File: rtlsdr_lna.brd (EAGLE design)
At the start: 34.6 x 11.7 mm, 18 parts, among them U1 MIC5205-3

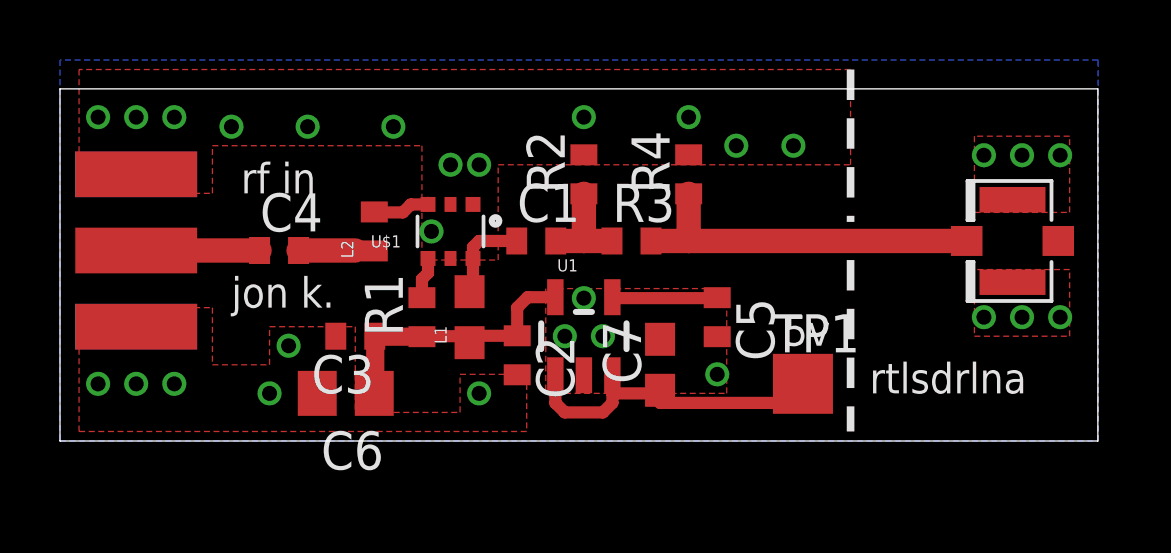
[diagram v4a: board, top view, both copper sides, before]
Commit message: cleaned up layout to pass DRC, rtl-sdr-lna ready for manufacturing
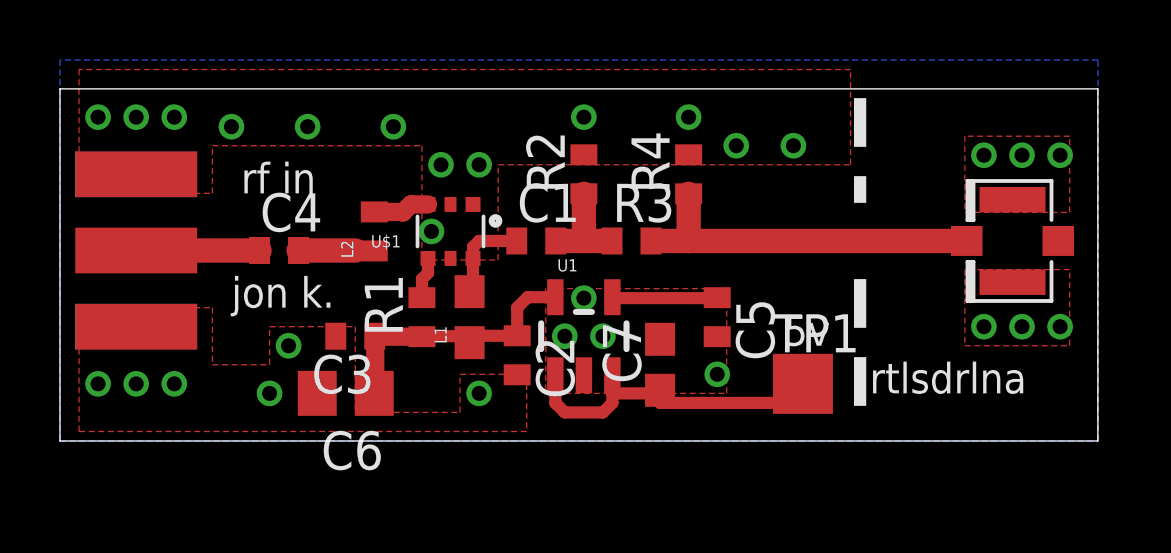
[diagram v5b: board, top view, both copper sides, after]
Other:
- board text removed: "copper tape may be helpful"
- board text removed: "cut here"
- board text removed: "solder edge of board to rf connector footprint"
- board text removed: "soldermask removed on board edges"
- board text removed: "units in mm"
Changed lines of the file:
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@@
 <wire x1="34.595" y1="11.7375" x2="0" y2="11.7375" width="0" layer="20"/>
 <wire x1="0" y1="11.7375" x2="0" y2="0" width="0" layer="20"/>
-<wire x1="26.3525" y1="12.3825" x2="26.3525" y2="7.3025" width="0.254" layer="121" style="shortdash"/>
-<wire x1="26.3525" y1="6.0325" x2="26.3525" y2="0.3175" width="0.254" layer="121" style="shortdash"/>
-<rectangle x1="22.86" y1="5.715" x2="29.21" y2="7.62" layer="29"/>
+<rectangle x1="21.9075" y1="5.715" x2="28.2575" y2="7.62" layer="29"/>
 <rectangle x1="0.3175" y1="10.16" x2="26.3525" y2="11.43" layer="30"/>
 <rectangle x1="0.3175" y1="0" x2="15.5575" y2="0.9525" layer="29"/>
@@
 <rectangle x1="14.605" y1="10.16" x2="26.3525" y2="11.7475" layer="29"/>
 <rectangle x1="2.8575" y1="10.16" x2="14.605" y2="11.7475" layer="29"/>
-<text x="24.13" y="13.0175" size="0.8128" layer="47" font="vector">cut here</text>
-<dimension x1="0" y1="0" x2="0" y2="11.7475" x3="-1.5875" y3="5.87375" layer="47"/>
-<dimension x1="0" y1="19.685" x2="26.3525" y2="19.685" x3="13.17625" y3="18.0975" layer="47"/>
-<text x="5.3975" y="24.4475" size="1.778" layer="47" font="vector">units in mm</text>
-<text x="-6.6675" y="-7.9375" size="1.27" layer="47" font="vector">soldermask removed on board edges</text>
-<text x="-6.6675" y="-10.795" size="1.27" layer="47" font="vector">solder edge of board to rf connector footprint</text>
-<text x="-6.6675" y="-13.6525" size="1.27" layer="47" font="vector">copper tape may be helpful</text>
+<wire x1="26.67" y1="11.43" x2="26.67" y2="7.9375" width="0.4064" layer="121" style="shortdash"/>
+<wire x1="26.67" y1="5.3975" x2="26.67" y2="0.3175" width="0.4064" layer="121" style="shortdash"/>
 </plain>
 <attributes>
@@
 Einstellungen hier und speichern die Design Rules unter
 einem neuen Namen ab.</description>
-<description language="en">&lt;b&gt;EAGLE Design Rules&lt;/b&gt;
+<description language="en">&lt;b&gt;Laen's PCB Order Design Rules&lt;/b&gt;
 &lt;p&gt;
-The default Design Rules have been set to cover
-a wide range of applications. Your particular design
-may have different requirements, so please make the
-necessary adjustments and save your customized
-design rules under a new name.</description>
-<description language="zh">&lt;b&gt;Seeed Studio EAGLE Design Rules&lt;/b&gt;
-</description>
+Please make sure your boards conform to these design rules.</description>
 <param name="layerSetup" value="(1*16)"/>
-<param name="mtCopper" value="0.035mm 0.035mm 0.035mm 0.035mm 0.035mm 0.035mm 0.035mm 0.035mm 0.035mm 0.035mm 0.035mm 0.035mm 0.035mm 0.035mm 0.035mm 0.035mm"/>
-<param name="mtIsolate" value="1.5mm 0.15mm 0.2mm 0.15mm 0.2mm 0.15mm 0.2mm 0.15mm 0.2mm 0.15mm 0.2mm 0.15mm 0.2mm 0.15mm 0.2mm"/>
-<param name="mdWireWire" value="7mil"/>
-<param name="mdWirePad" value="7mil"/>
-<param name="mdWireVia" value="7mil"/>
-<param name="mdPadPad" value="7mil"/>
-<param name="mdPadVia" value="7mil"/>
-<param name="mdViaVia" value="7mil"/>
-<param name="mdSmdPad" value="0mil"/>
-<param name="mdSmdVia" value="0mil"/>
-<param name="mdSmdSmd" value="0mil"/>
+<param name="mtCopper" value="0.0356mm 0.0356mm 0.0356mm 0.0356mm 0.0356mm 0.0356mm 0.0356mm 0.0356mm 0.0356mm 0.0356mm 0.0356mm 0.0356mm 0.0356mm 0.0356mm 0.0356mm 0.0356mm"/>
+<param name="mtIsolate" value="1.5011mm 0.1499mm 0.2007mm 0.1499mm 0.2007mm 0.1499mm 0.2007mm 0.1499mm 0.2007mm 0.1499mm 0.2007mm 0.1499mm 0.2007mm 0.1499mm 0.2007mm"/>
+<param name="mdWireWire" value="6mil"/>
+<param name="mdWirePad" value="6mil"/>
+<param name="mdWireVia" value="6mil"/>
+<param name="mdPadPad" value="6mil"/>
+<param name="mdPadVia" value="6mil"/>
+<param name="mdViaVia" value="6mil"/>
+<param name="mdSmdPad" value="6mil"/>
+<param name="mdSmdVia" value="6mil"/>
+<param name="mdSmdSmd" value="6mil"/>
 <param name="mdViaViaSameLayer" value="8mil"/>
 <param name="mnLayersViaInSmd" value="2"/>
-<param name="mdCopperDimension" value="10mil"/>
-<param name="mdDrill" value="10mil"/>
+<param name="mdCopperDimension" value="15mil"/>
+<param name="mdDrill" value="6mil"/>
 <param name="mdSmdStop" value="0mil"/>
-<param name="msWidth" value="8mil"/>
-<param name="msDrill" value="12mil"/>
-<param name="msMicroVia" value="12mil"/>
+<param name="msWidth" value="6mil"/>
+<param name="msDrill" value="13mil"/>
+<param name="msMicroVia" value="13mil"/>
 <param name="msBlindViaRatio" value="0.5"/>
 <param name="rvPadTop" value="0.25"/>
@@
 <param name="rvMicroViaOuter" value="0.25"/>
 <param name="rvMicroViaInner" value="0.25"/>
-<param name="rlMinPadTop" value="12mil"/>
+<param name="rlMinPadTop" value="7mil"/>
 <param name="rlMaxPadTop" value="20mil"/>
-<param name="rlMinPadInner" value="12mil"/>
+<param name="rlMinPadInner" value="7mil"/>
 <param name="rlMaxPadInner" value="20mil"/>
-<param name="rlMinPadBottom" value="12mil"/>
+<param name="rlMinPadBottom" value="7mil"/>
 <param name="rlMaxPadBottom" value="20mil"/>
-<param name="rlMinViaOuter" value="6mil"/>
+<param name="rlMinViaOuter" value="7mil"/>
 <param name="rlMaxViaOuter" value="20mil"/>
-<param name="rlMinViaInner" value="6mil"/>
+<param name="rlMinViaInner" value="7mil"/>
 <param name="rlMaxViaInner" value="20mil"/>
 <param name="rlMinMicroViaOuter" value="4mil"/>
@@
 <param name="psTop" value="-1"/>
 <param name="psBottom" value="-1"/>
-<param name="psFirst" value="0"/>
+<param name="psFirst" value="-1"/>
 <param name="psElongationLong" value="100"/>
 <param name="psElongationOffset" value="100"/>
 <param name="mvStopFrame" value="1"/>
 <param name="mvCreamFrame" value="0"/>
-<param name="mlMinStopFrame" value="3mil"/>
-<param name="mlMaxStopFrame" value="3mil"/>
+<param name="mlMinStopFrame" value="4mil"/>
+<param name="mlMaxStopFrame" value="4mil"/>
 <param name="mlMinCreamFrame" value="0mil"/>
 <param name="mlMaxCreamFrame" value="0mil"/>
-<param name="mlViaStopLimit" value="100mil"/>
+<param name="mlViaStopLimit" value="0mil"/>
 <param name="srRoundness" value="0"/>
 <param name="srMinRoundness" value="0mil"/>
@@
 <param name="checkAngle" value="0"/>
 <param name="checkFont" value="1"/>
-<param name="checkRestrict" value="0"/>
+<param name="checkRestrict" value="1"/>
 <param name="useDiameter" value="13"/>
 <param name="maxErrors" value="50"/>
@@
 <via x="1.27" y="10.795" extent="1-16" drill="0.5"/>
 <via x="2.54" y="10.795" extent="1-16" drill="0.5"/>
-<via x="13.0175" y="9.2075" extent="1-16" drill="0.5"/>
+<via x="12.7" y="9.2075" extent="1-16" drill="0.5"/>
 <via x="12.3825" y="6.985" extent="1-16" drill="0.5"/>
 <via x="13.97" y="9.2075" extent="1-16" drill="0.5"/>
@@
 <via x="13.97" y="1.5875" extent="1-16" drill="0.5"/>
 <polygon width="0.254" layer="1">
-<vertex x="30.48" y="5.715"/>
-<vertex x="30.48" y="3.4925"/>
-<vertex x="33.655" y="3.4925"/>
+<vertex x="30.1625" y="5.715"/>
+<vertex x="30.1625" y="3.175"/>
+<vertex x="33.655" y="3.175"/>
 <vertex x="33.655" y="5.715"/>
 </polygon>
 <polygon width="0.254" layer="1">
-<vertex x="30.48" y="10.16"/>
-<vertex x="30.48" y="7.62"/>
+<vertex x="30.1625" y="10.16"/>
+<vertex x="30.1625" y="7.62"/>
 <vertex x="33.655" y="7.62"/>
 <vertex x="33.655" y="10.16"/>
@@
 <via x="32.0675" y="9.525" extent="1-16" drill="0.5"/>
 <via x="33.3375" y="9.525" extent="1-16" drill="0.5"/>
-<via x="30.7975" y="4.1275" extent="1-16" drill="0.5"/>
-<via x="32.0675" y="4.1275" extent="1-16" drill="0.5"/>
-<via x="33.3375" y="4.1275" extent="1-16" drill="0.5"/>
+<via x="30.7975" y="3.81" extent="1-16" drill="0.5"/>
+<via x="32.0675" y="3.81" extent="1-16" drill="0.5"/>
+<via x="33.3375" y="3.81" extent="1-16" drill="0.5"/>
 <contactref element="C7" pad="2"/>
 <via x="11.1125" y="10.4775" extent="1-16" drill="0.5"/>
@@
 <contactref element="U$1" pad="3"/>
 <wire x1="12.2675" y1="7.9375" x2="12.2675" y2="7.885" width="0.4064" layer="1"/>
-<wire x1="12.2675" y1="7.885" x2="11.695" y2="7.885" width="0.4064" layer="1"/>
-<wire x1="11.695" y1="7.885" x2="11.43" y2="7.62" width="0.4064" layer="1"/>
-<wire x1="11.43" y1="7.62" x2="10.4775" y2="7.62" width="0.4064" layer="1"/>
-<wire x1="10.4775" y1="7.62" x2="10.4775" y2="7.635" width="0.4064" layer="1"/>
+<wire x1="10.4775" y1="7.635" x2="11.43" y2="7.635" width="0.6096" layer="1"/>
+<wire x1="12.2675" y1="7.885" x2="11.695" y2="7.885" width="0.6096" layer="1"/>
+<wire x1="11.695" y1="7.885" x2="11.43" y2="7.62" width="0.6096" layer="1"/>
+<wire x1="11.43" y1="7.635" x2="11.43" y2="7.62" width="0.6096" layer="1"/>
 </signal>
 </signals>
+<errors>
+</errors>
 </board>
 </drawing>
